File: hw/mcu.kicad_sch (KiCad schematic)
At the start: 13 parts, among them J1 Prog/debug, U1 STM32L432KBUx, U6 ZD25WQ16CTIGT, Y1 32768 Hz

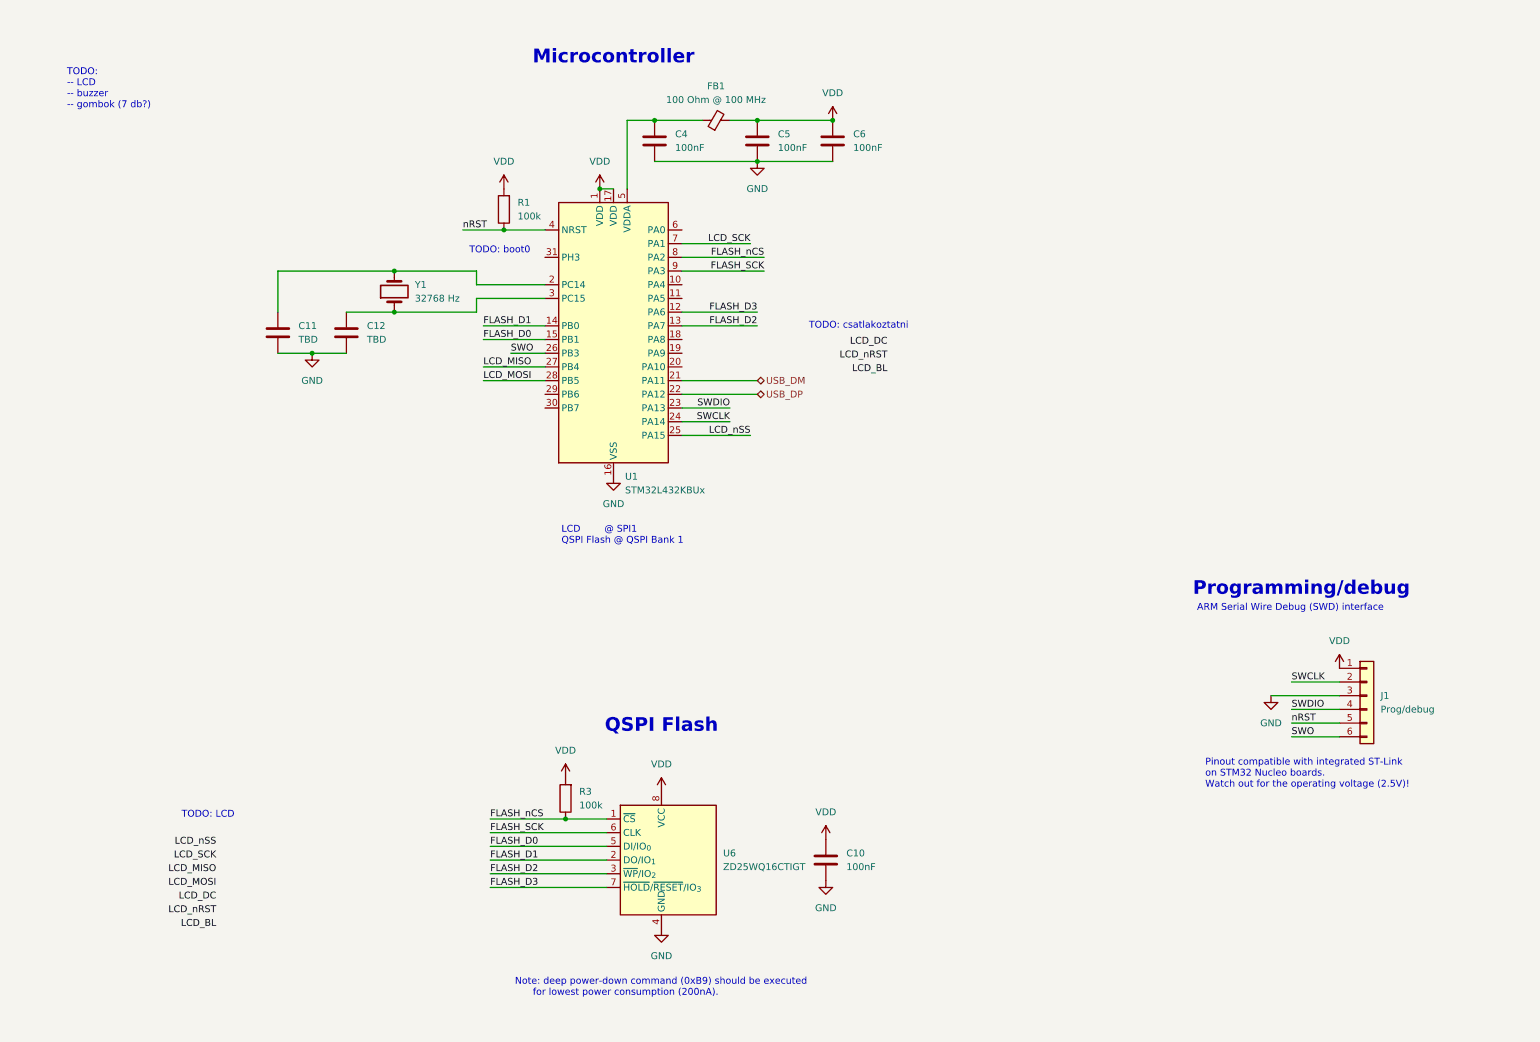
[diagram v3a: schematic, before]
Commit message: Schematic is finished. Needs some touch-ups and component selection (esp. for switches).
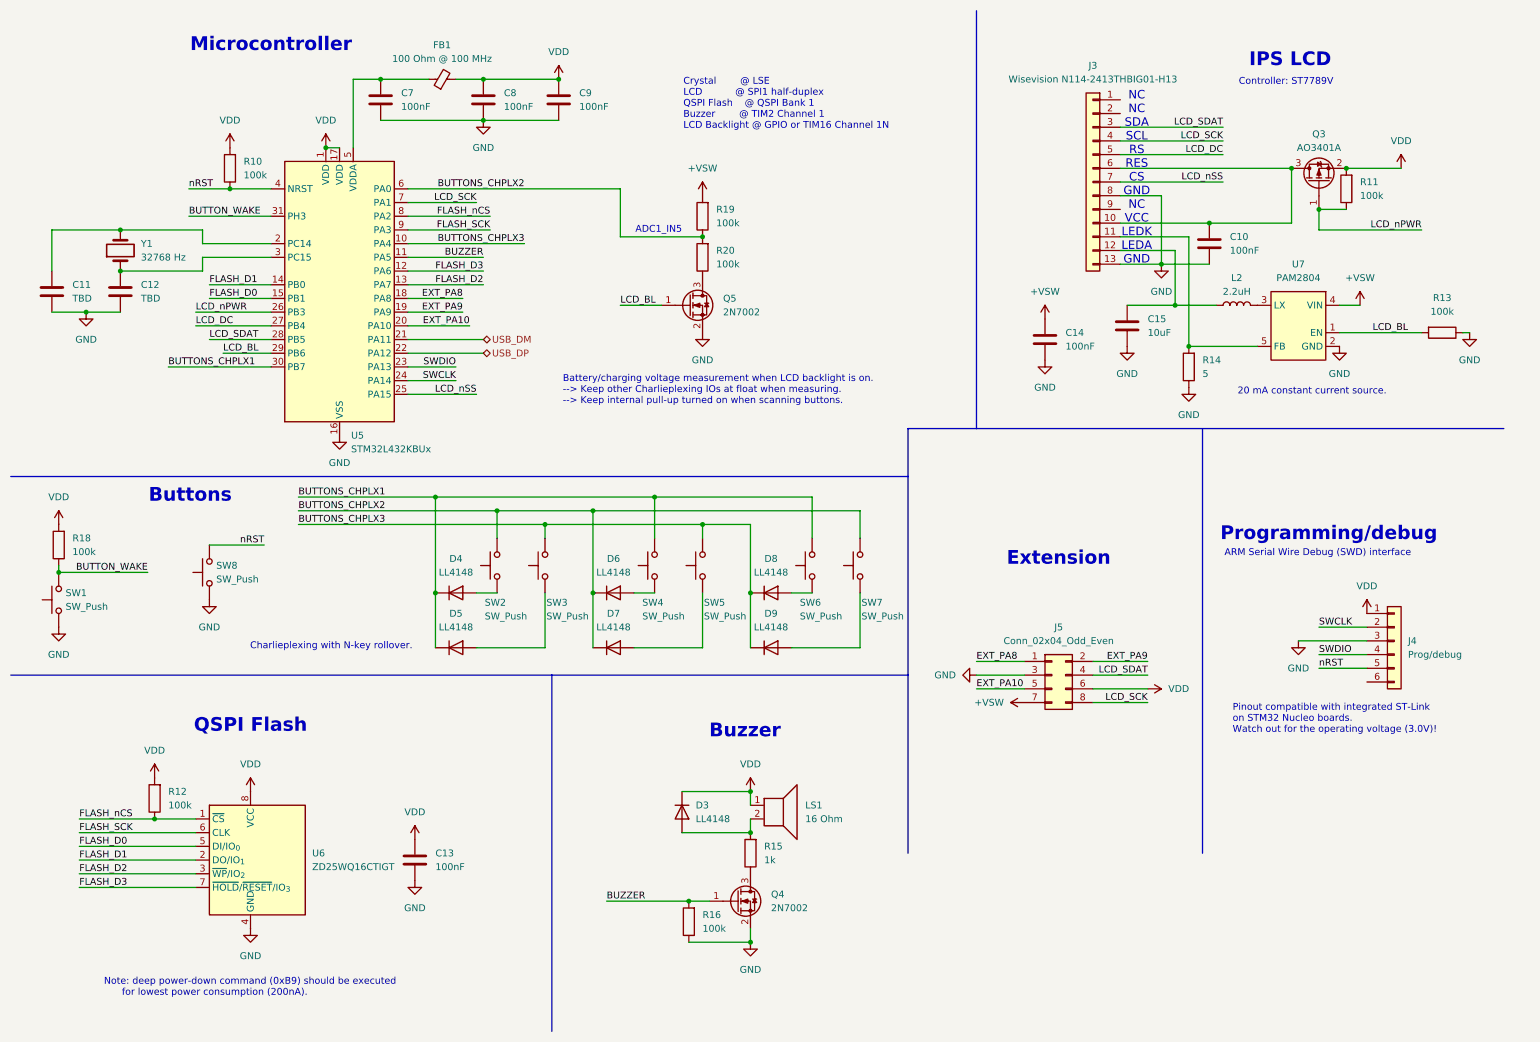
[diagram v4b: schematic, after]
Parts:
- added C10, C14: 100nF, Capacitor_SMD:C_0805_2012Metric, symbol Device:C
- added C15: 10uF, Capacitor_SMD:C_1206_3216Metric, symbol Device:C
- added D3, D4, D5, D6, D7, D8, D9: LL4148, Diode_SMD:D_MiniMELF, symbol Diode:LL4148
- added J3: Wisevision N114-2413THBIG01-H13, symbol Connector_Generic:Conn_01x13
- added J5: Conn_02x04_Odd_Even, symbol Connector_Generic:Conn_02x04_Odd_Even
- added L2: 2.2uH, symbol Device:L
- added LS1: 16 Ohm, Buzzer_Beeper:MagneticBuzzer_CUI_CMT-8504-100-SMT, symbol Device:Speaker
- added Q3: AO3401A, Package_TO_SOT_SMD:SOT-23, symbol Transistor_FET:AO3401A
- added Q4, Q5: 2N7002, Package_TO_SOT_SMD:SOT-23, symbol Transistor_FET:2N7002
- added R11, R13, R16, R18, R19, R20: 100k, Resistor_SMD:R_0805_2012Metric, symbol Device:R
- added R14: 5, Resistor_SMD:R_0805_2012Metric, symbol Device:R
- added R15: 1k, Resistor_SMD:R_0805_2012Metric, symbol Device:R
- added SW1, SW2, SW3, SW4, SW5, SW6, SW7, SW8: SW_Push, symbol Switch:SW_Push
- added U7: PAM2804, Package_TO_SOT_SMD:SOT-23-5, symbol sem18:LN2401-TP
- renumbered C10 to C13, C4 to C7, C5 to C8, C6 to C9, J1 to J4, R1 to R10, R3 to R12, U1 to U5
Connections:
- net LCD_MISO is gone; now on net LCD_DC: U5.27 (PB4)
- net GND: now also C10.1, C14.1, C15.2, J3.13 (Pin_13), J3.8 (Pin_8), J5.3 (Pin_3), Q4.2 (S), Q5.2 (S), R13.1, R14.1, R16.1, SW1.1, SW8.1, U7.2 (GND)
- net LCD_BL: now also U5.29 (PB6), Q5.1 (G), R13.2, U7.1 (EN)
- net LCD_DC: now also J3.5 (Pin_5)
- net LCD_SCK: now also J3.4 (Pin_4), J5.8 (Pin_8)
- net LCD_nSS: now also J3.7 (Pin_7)
- net VDD: now also D3.1 (K), J5.6 (Pin_6), LS1.1, Q3.2 (S), R11.2, R18.2
- net nRST: now also SW8.2
- net BUTTONS_CHPLX3: now reaches U5.10 (PA4)
- net BUTTONS_CHPLX3: now also D8.1 (K), D9.1 (K), SW3.2, SW5.2
- net BUZZER: now reaches U5.11 (PA5)
- net BUZZER: now also Q4.1 (G), R16.2
- net EXT_PA8: now reaches U5.18 (PA8)
- net EXT_PA8: now also J5.1 (Pin_1)
- net EXT_PA9: now reaches U5.19 (PA9)
- net EXT_PA9: now also J5.2 (Pin_2)
- net EXT_PA10: now reaches U5.20 (PA10)
- net EXT_PA10: now also J5.5 (Pin_5)
- net BUTTONS_CHPLX1: now reaches U5.30 (PB7)
- net BUTTONS_CHPLX1: now also D4.1 (K), D5.1 (K), SW4.2, SW6.2
- net BUTTON_WAKE: now reaches U5.31 (PH3)
- net BUTTON_WAKE: now also R18.1, SW1.2
- net BUTTONS_CHPLX2: now reaches U5.6 (PA0)
- net BUTTONS_CHPLX2: now also D6.1 (K), D7.1 (K), R19.1, R20.2, SW2.2, SW7.2
- net LCD_MOSI renamed LCD_SDAT
- net LCD_SDAT: now also J3.3 (Pin_3), J5.4 (Pin_4)
- net SWO: no longer names the net of J4.6 (Pin_6)
- net SWO: no longer U5.26 (PB3)
- new net: C10.2, J3.10 (Pin_10), J3.6 (Pin_6), Q3.3 (D)
- new net: L2.2, U7.3 (LX)
- new net: J3.11 (Pin_11), R14.2, U7.5 (FB)
- new net: Q4.3 (D), R15.1
- new net: C15.1, J3.12 (Pin_12), L2.1
- new net: D3.2 (A), LS1.2, R15.2
- new net: D9.2 (A), SW7.1
- new net: D6.2 (A), SW4.1
- new net: D4.2 (A), SW2.1
- new net: D5.2 (A), SW3.1
- new net: D8.2 (A), SW6.1
- new net: D7.2 (A), SW5.1
- new net: Q5.3 (D), R20.1
- new net +VSW: C14.2, J5.7 (Pin_7), R19.2, U7.4 (VIN)
- new net LCD_nPWR: Q3.1 (G), R11.1, U5.26 (PB3)
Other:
- note added: "20 mA constant current source."
- note added: "ADC1_IN5"
- note added: "Battery/charging voltage measurement when LCD backlight is on. --> Keep other Charlieplexing IOs at float when measuring. --> Keep internal pull-up turned on when scanning buttons."
- note added: "Buttons"
- note added: "Buzzer"
- note added: "Charlieplexing with N-key rollover."
- note added: "Controller: ST7789V"
- note added: "Crystal @ LSE LCD @ SPI1 half-duplex QSPI Flash @ QSPI Bank 1 Buzzer @ TIM2 Channel 1 LCD Backlight @ GPIO or TIM16 Channel 1N"
- note added: "Extension"
- note added: "IPS LCD"
- note added: "NC NC SDA SCL RS RES CS GND NC VCC LEDK LEDA GND"
- note added: "Pinout compatible with integrated ST-Link on STM32 Nucleo boards. Watch out for the operating voltage (3.0V)!"
- note removed: "LCD @ SPI1 QSPI Flash @ QSPI Bank 1"
- note removed: "Pinout compatible with integrated ST-Link on STM32 Nucleo boards. Watch out for the operating voltage (2.5V)!"
- note removed: "TODO: -- LCD -- buzzer -- gombok (7 db?)"
- note removed: "TODO: LCD"
- note removed: "TODO: boot0"
- note removed: "TODO: csatlakoztatni"
- moved on the sheet: C11, C12, C13, C7, C8, C9, FB1, J4, R10, R12, U5, U6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

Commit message: WIP
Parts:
- removed D6, D7, D8, D9: LL4148, Diode_SMD:D_MiniMELF, symbol Diode:LL4148
- removed SW1, SW2, SW3, SW4, SW5, SW6, SW7: SW_Push, symbol Switch:SW_Push
- added SW1, SW2, SW3: SW_Push_Shielded, sem18:SMD_Tactile_Switch_7.7x3.6mm_Right-angle, symbol Switch:SW_Push_Shielded
- added SW4: ~, sem18:SMD_Directional_Switch, symbol sem18:SW_DIR_6p
- C10, C11, C12, C13, C14, C7, C8, C9: footprint Capacitor_SMD:C_0805_2012Metric -> Capacitor_SMD:C_0603_1608Metric
- J5: footprint (none) -> Connector_PinHeader_2.54mm:PinHeader_2x04_P2.54mm_Vertical
- L2: footprint (none) -> Inductor_SMD:L_APV_ANR3012
- R10, R11, R12, R13, R14, R15, R16, R18, R19, R20: footprint Resistor_SMD:R_0805_2012Metric -> Resistor_SMD:R_0603_1608Metric
- Y1: footprint (none) -> Crystal:Crystal_DS26_D2.0mm_L6.0mm_Vertical
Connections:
- net BUTTONS_CHPLX2: now also SW2.2
- net BUTTONS_CHPLX3: now also SW3.2
- net BUTTON_WAKE: now also SW1.2
- net GND: now also SW1.1, SW1.SH (B), SW2.SH (B), SW3.SH (B)
- net at D4.2 (A): now also SW2.1
- net at D5.2 (A): now also SW3.1

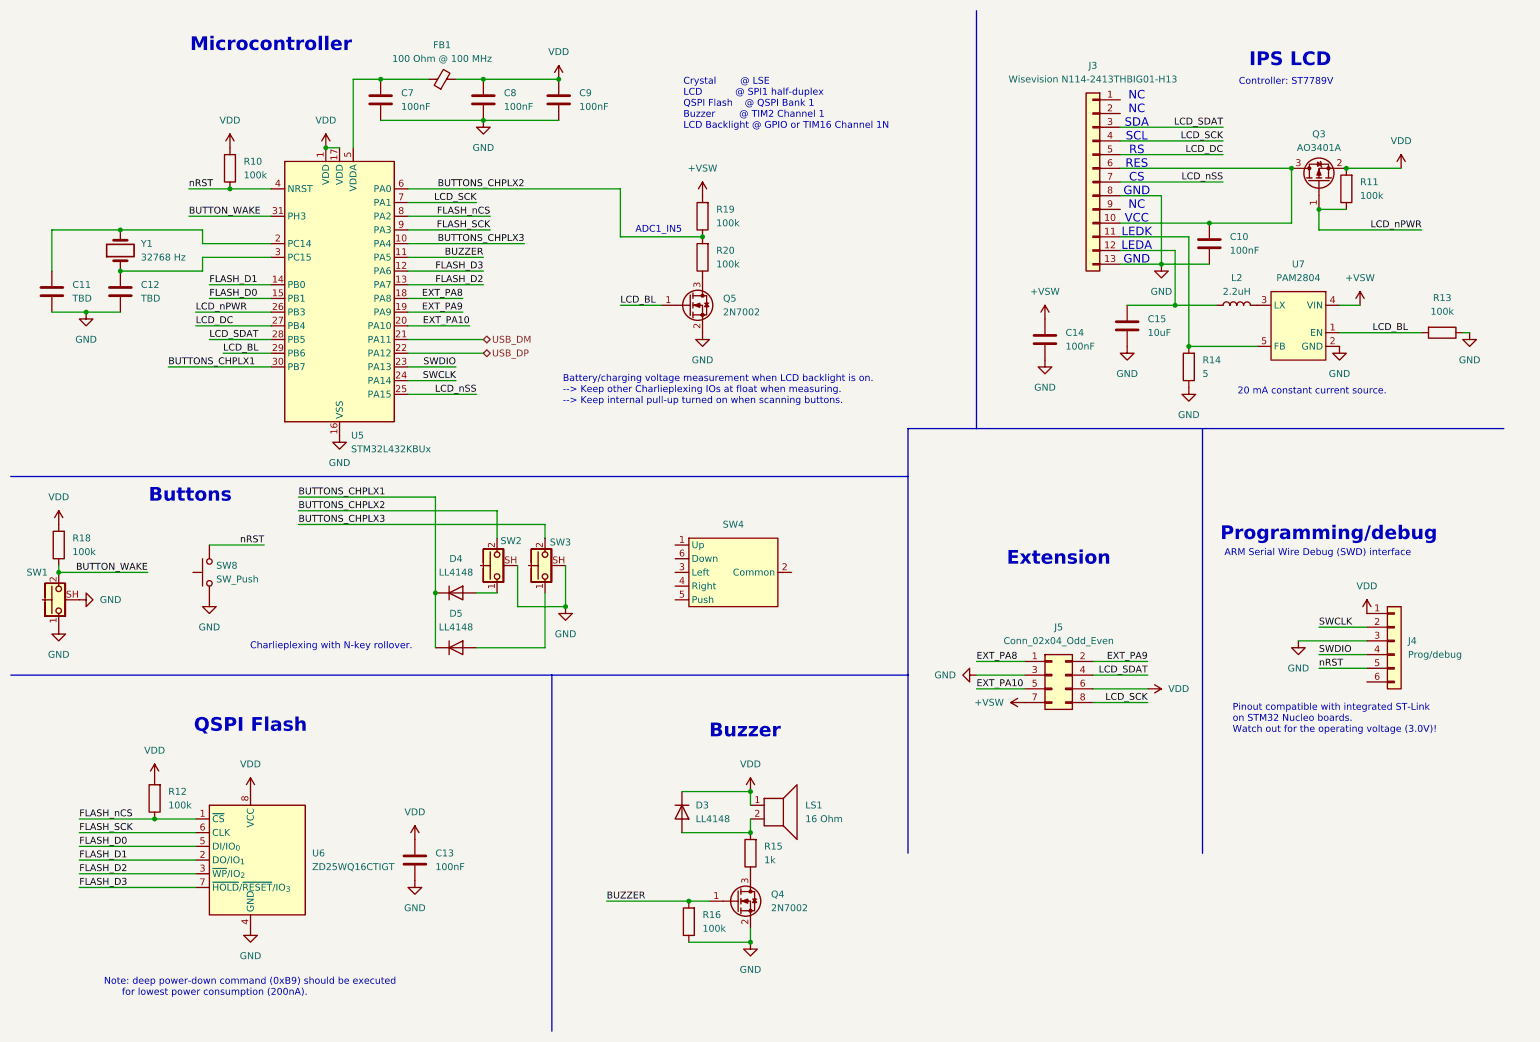
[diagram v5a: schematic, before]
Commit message: Different microcontroller. Placed most of the components too.
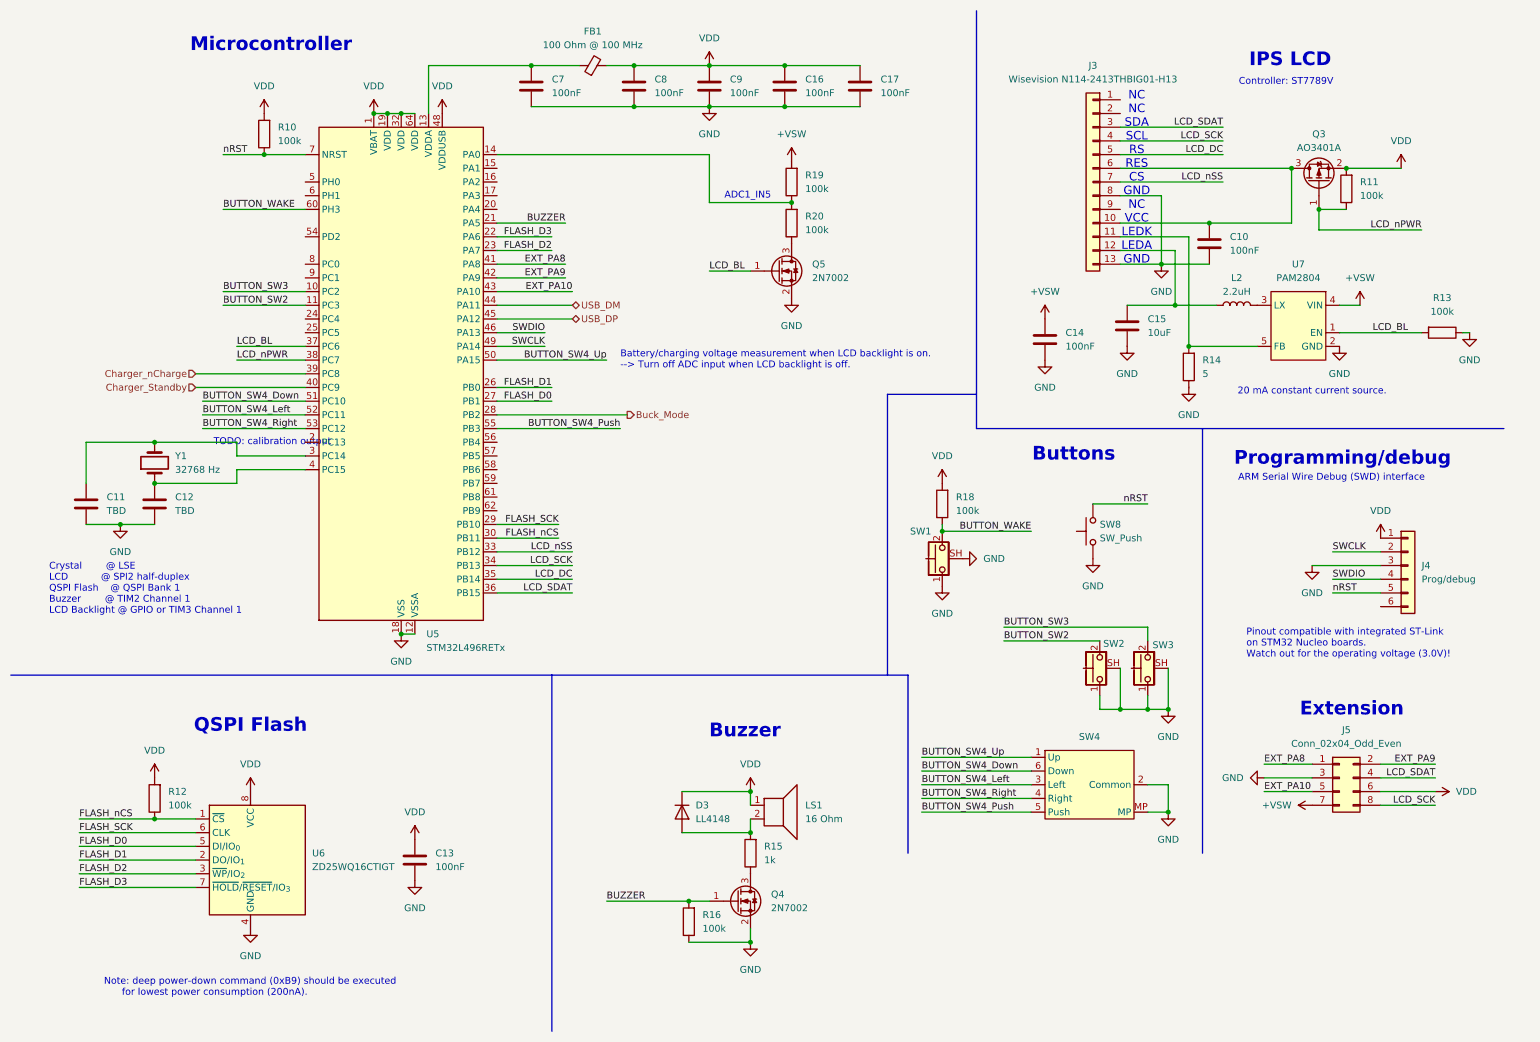
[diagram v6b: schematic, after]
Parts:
- removed D4, D5: LL4148, Diode_SMD:D_MiniMELF, symbol Diode:LL4148
- removed U5: STM32L432KBUx, Package_DFN_QFN:QFN-32-1EP_5x5mm_P0.5mm_EP3.45x3.45mm, symbol MCU_ST_STM32L4:STM32L432KBUx
- added C16, C17: 100nF, Capacitor_SMD:C_0603_1608Metric, symbol Device:C
- added U5: STM32L496RETx, Package_QFP:LQFP-64_10x10mm_P0.5mm, symbol MCU_ST_STM32L4:STM32L496RETx
- C15: footprint Capacitor_SMD:C_1206_3216Metric -> Capacitor_SMD:C_0805_2012Metric
- J3: footprint (none) -> sem18:LCD_ST7789V_13pin
- U6: footprint Package_SO:SOIC-8_3.9x4.9mm_P1.27mm -> Package_SO:SOIC-8_5.3x5.3mm_P1.27mm
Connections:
- net BUTTON_WAKE: now also U5.60 (PH3)
- net BUZZER: now also U5.21 (PA5)
- net EXT_PA10: now also U5.43 (PA10)
- net EXT_PA8: now also U5.41 (PA8)
- net EXT_PA9: now also U5.42 (PA9)
- net FLASH_D0: now also U5.27 (PB1)
- net FLASH_D1: now also U5.26 (PB0)
- net FLASH_D2: now also U5.23 (PA7)
- net FLASH_D3: now also U5.22 (PA6)
- net FLASH_SCK: now also U5.29 (PB10)
- net FLASH_nCS: now also U5.30 (PB11)
- net GND: now also SW2.1, SW3.1, SW4.2 (Common), SW4.MP, C16.1, C17.1, U5.12 (VSSA), U5.18 (VSS), U5.31 (VSS), U5.47 (VSS), U5.63 (VSS)
- net LCD_BL: now also U5.37 (PC6)
- net LCD_DC: now also U5.35 (PB14)
- net LCD_SCK: now also U5.34 (PB13)
- net LCD_SDAT: now also U5.36 (PB15)
- net LCD_nPWR: now also U5.38 (PC7)
- net LCD_nSS: now also U5.33 (PB12)
- net SWCLK: now also U5.49 (PA14)
- net SWDIO: now also U5.46 (PA13)
- net USB_DM: now also U5.44 (PA11)
- net USB_DP: now also U5.45 (PA12)
- net VDD: now also C16.2, C17.2, U5.1 (VBAT), U5.19 (VDD), U5.32 (VDD), U5.48 (VDDUSB), U5.64 (VDD)
- net nRST: now also U5.7 (NRST)
- net at C11.2, Y1.2: now also U5.3 (PC14)
- net at C12.2, Y1.1: now also U5.4 (PC15)
- net at C7.2, FB1.1: now also U5.13 (VDDA)
- net BUTTON_SW4_Up: now reaches SW4.1 (Up)
- net BUTTON_SW4_Up: now also U5.50 (PA15)
- net BUTTON_SW4_Left: now reaches SW4.3 (Left)
- net BUTTON_SW4_Left: now also U5.52 (PC11)
- net BUTTON_SW4_Right: now reaches SW4.4 (Right)
- net BUTTON_SW4_Right: now also U5.53 (PC12)
- net BUTTON_SW4_Push: now reaches SW4.5 (Push)
- net BUTTON_SW4_Push: now also U5.55 (PB3)
- net BUTTON_SW4_Down: now reaches SW4.6 (Down)
- net BUTTON_SW4_Down: now also U5.51 (PC10)
- net BUTTONS_CHPLX2: no longer names the net of R19.1, R20.2
- net BUTTONS_CHPLX2: now also U5.14 (PA0); no longer SW2.2
- net BUTTONS_CHPLX3 renamed BUTTON_SW3
- net BUTTON_SW3: now also U5.10 (PC2)
- new net BUTTON_SW2: SW2.2, U5.11 (PC3)
- new net Buck_Mode: U5.28 (PB2)
- new net Charger_Standby: U5.40 (PC9)
- new net Charger_nCharge: U5.39 (PC8)
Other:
- note added: "Battery/charging voltage measurement when LCD backlight is on. --> Turn off ADC input when LCD backlight is off."
- note added: "Crystal @ LSE LCD @ SPI2 half-duplex QSPI Flash @ QSPI Bank 1 Buzzer @ TIM2 Channel 1 LCD Backlight @ GPIO or TIM3 Channel 1"
- note added: "TODO: calibration output"
- note removed: "Battery/charging voltage measurement when LCD backlight is on. --> Keep other Charlieplexing IOs at float when measuring. --> Keep internal pull-up turned on when scanning buttons."
- note removed: "Charlieplexing with N-key rollover."
- note removed: "Crystal @ LSE LCD @ SPI1 half-duplex QSPI Flash @ QSPI Bank 1 Buzzer @ TIM2 Channel 1 LCD Backlight @ GPIO or TIM16 Channel 1N"
- moved on the sheet: C11, C12, C7, C8, C9, FB1, J4, J5, Q5, R10, R18, R19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
